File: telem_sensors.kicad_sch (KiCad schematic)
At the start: 45 parts, among them J4 Thermistor Molex, J5 Thermistor Molex, J6 Thermistor Molex, J7 Thermistor Molex, U4 LSM6DSRXTR, U5 MCP6L01x-xLT, U6 MCP6L01x-xLT, U7 BMP585, U8 MCP6L01x-xLT, U9 MCP6L01x-xLT

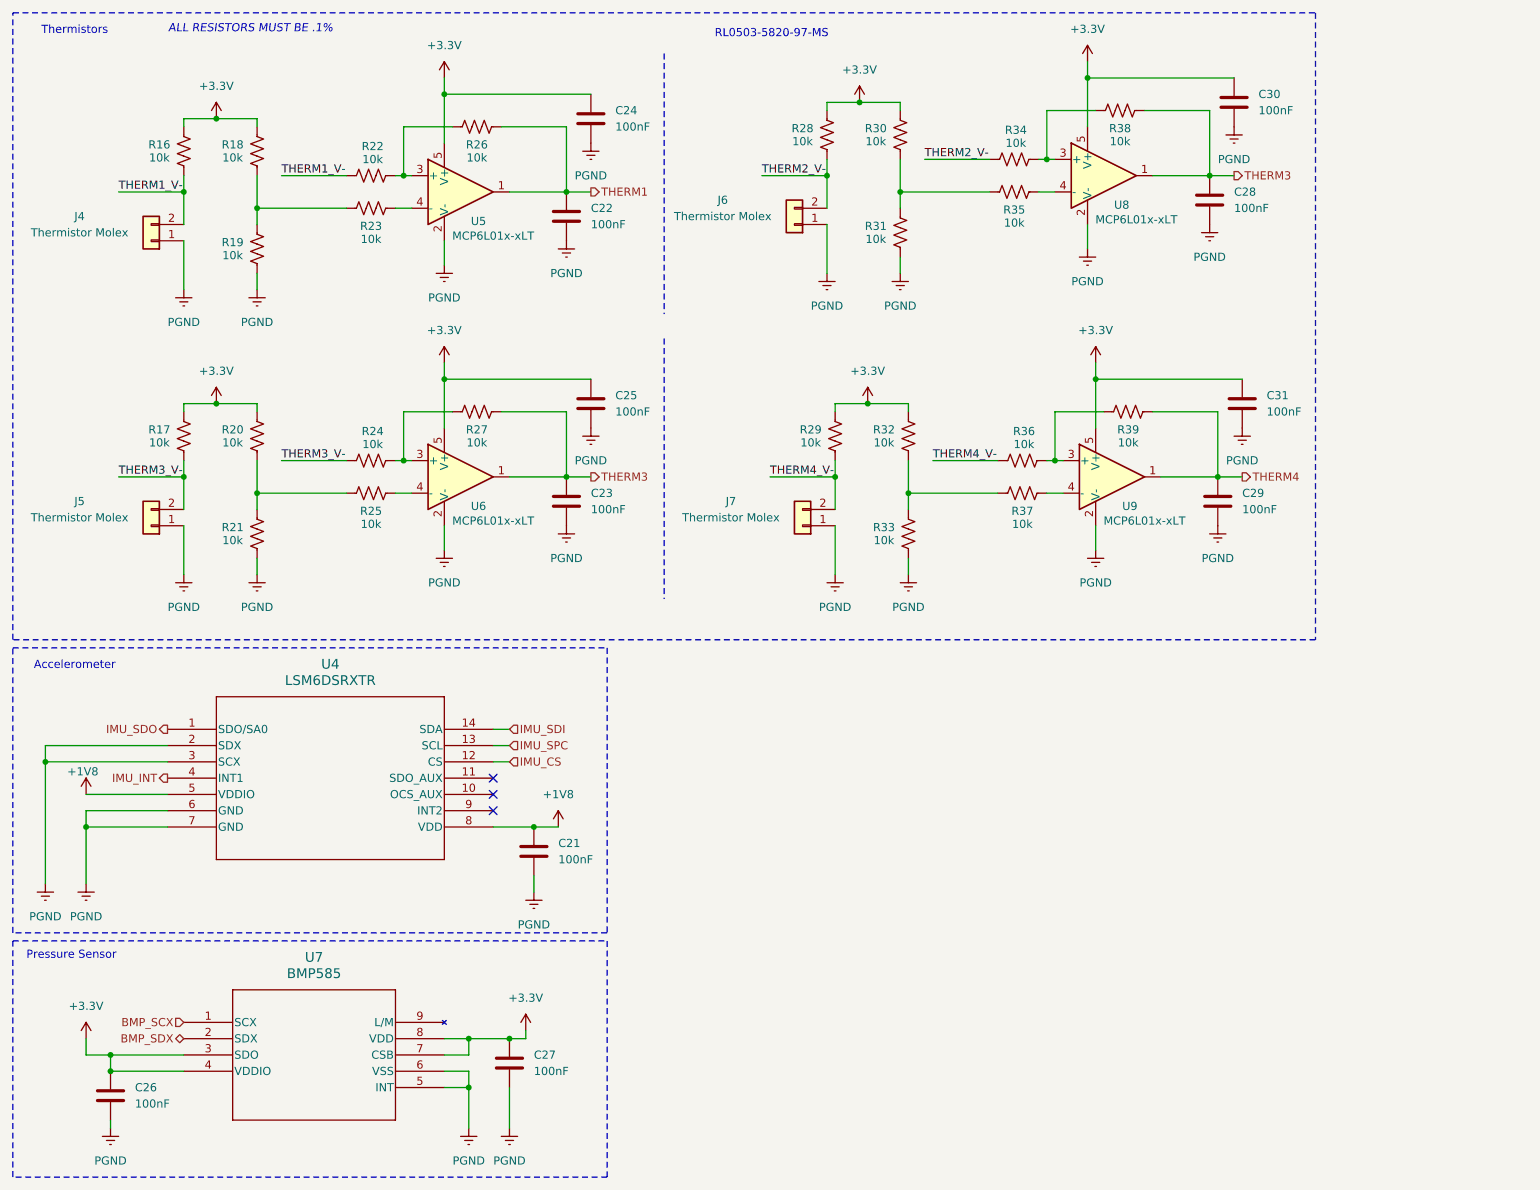
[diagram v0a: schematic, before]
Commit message: Added MAX-M10S GPS, selected antenna and did schematic
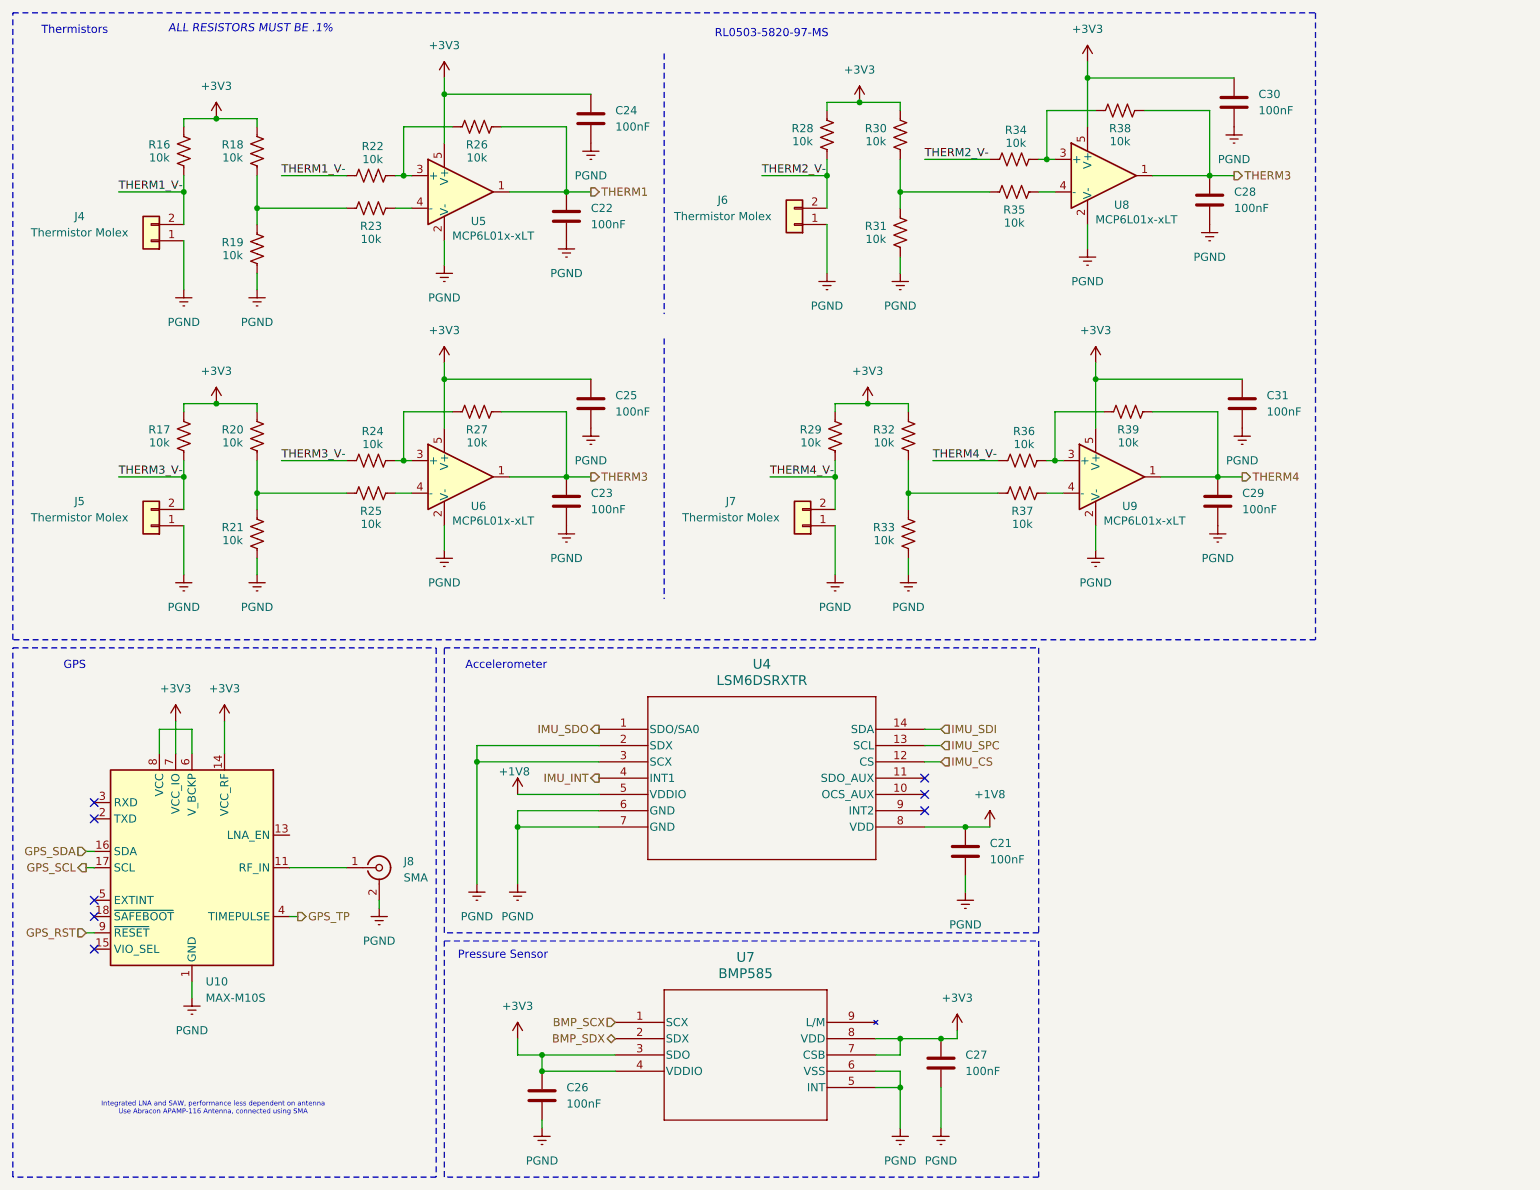
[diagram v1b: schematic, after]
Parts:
- added J8: SMA, Connector_Coaxial:SMA_Amphenol_132289_EdgeMount, symbol Connector:Conn_Coaxial
- added U10: MAX-M10S, RF_GPS:ublox_MAX, symbol RF_GPS:MAX-M10S
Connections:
- net PGND: now also J8.2 (Ext), U10.1 (GND), U10.10 (GND), U10.12 (GND)
- net +3.3V renamed +3V3
- net +3V3: now also U10.14 (VCC_RF), U10.7 (VCC_IO)
- new net: J8.1 (In), U10.11 (RF_IN)
- new net: U10.6 (V_BCKP), U10.8 (VCC)
- new net GPS_RST: U10.9 (~{RESET})
- new net GPS_SCL: U10.17 (SCL)
- new net GPS_SDA: U10.16 (SDA)
- new net GPS_TP: U10.4 (TIMEPULSE)
- no-connect marks 3 -> 8
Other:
- note added: "GPS"
- note added: "Integrated LNA and SAW, performance less dependent on antenna Use Abracon APAMP-116 Antenna, connected using SMA"
- moved on the sheet: C21, C26, C27, U4, U7

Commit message: Schematics complete; Starting layout. Removed 2 thermistors, not necessary. Going to update website once layout starts
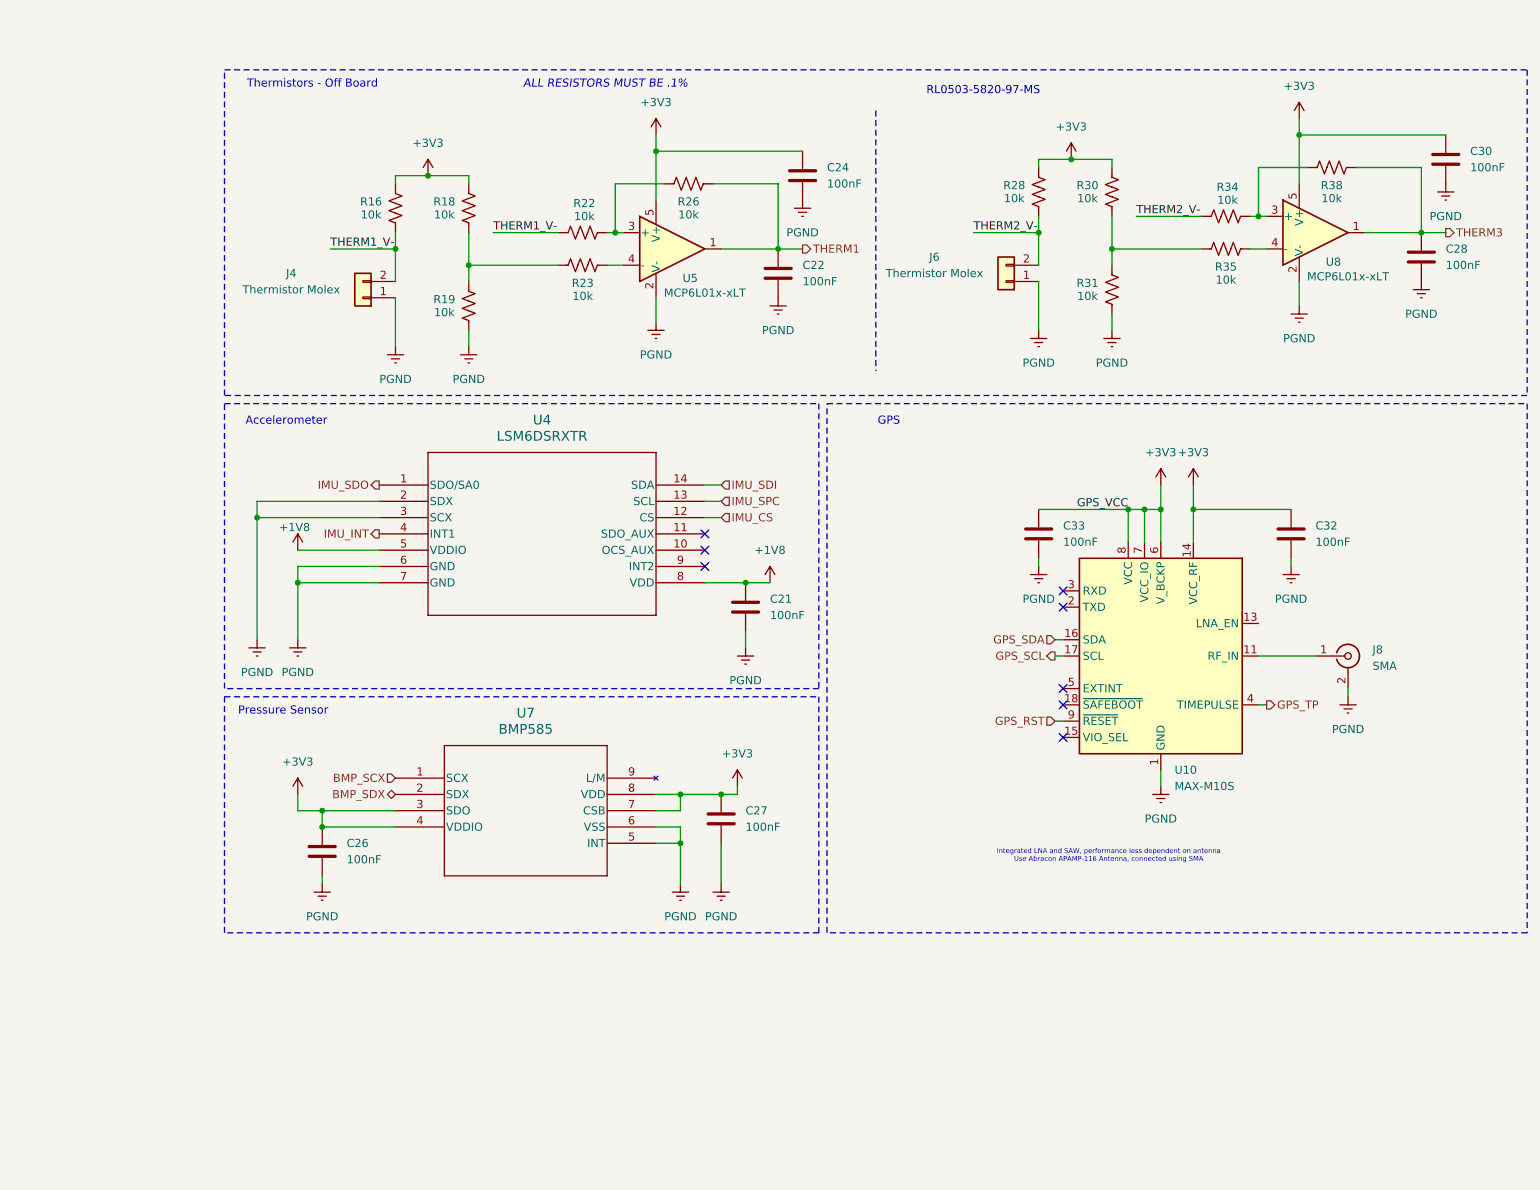
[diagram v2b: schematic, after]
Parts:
- removed C23, C25, C29, C31: 100nF, Capacitor_SMD:C_0805_2012Metric_Pad1.18x1.45mm_HandSolder, symbol Device:C
- removed J5, J7: Thermistor Molex, Connector_Molex:Molex_Micro-Fit_3.0_43650-0200_1x02_P3.00mm_Horizontal, symbol Connector_Generic:Conn_01x02
- removed R17, R20, R21, R24, R25, R27, R29, R32, R33, R36, R37, R39: 10k, Resistor_SMD:R_0603_1608Metric, symbol Device:R_US
- removed U6, U9: MCP6L01x-xLT, Package_TO_SOT_SMD:SOT-353_SC-70-5, symbol Amplifier_Operational:MCP6L01x-xLT
- added C32, C33: 100nF, Capacitor_SMD:C_0805_2012Metric_Pad1.18x1.45mm_HandSolder, symbol Device:C
- J4, J6: footprint Connector_Molex:Molex_Micro-Fit_3.0_43650-0200_1x02_P3.00mm_Horizontal -> Connector_Molex:Molex_MicroClasp_55935-0210_1x02_P2.00mm_Horizontal
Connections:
- net +3V3: now also U10.6 (V_BCKP), U10.8 (VCC), C32.1, C33.1
- net PGND: now also C32.2, C33.2
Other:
- note added: "Thermistors - Off Board"
- note removed: "Thermistors"
- moved on the sheet: C21, C22, C24, C26, C27, C28, C30, J4, J6, J8, R16, R18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

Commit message: Final schematic and initial layout
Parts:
- C21, C26, C27, C32, C33: footprint Capacitor_SMD:C_0805_2012Metric_Pad1.18x1.45mm_HandSolder -> Capacitor_SMD:C_0805_2012Metric
- C22, C24, C28, C30: footprint Capacitor_SMD:C_0805_2012Metric_Pad1.18x1.45mm_HandSolder -> Capacitor_SMD:C_0603_1608Metric
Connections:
- net PGND: now also J4.2 (Pin_2), J6.2 (Pin_2); no longer J4.1 (Pin_1), J6.1 (Pin_1)
- net THERM1_V-: now also J4.1 (Pin_1); no longer J4.2 (Pin_2)
- net THERM2_V-: now also J6.1 (Pin_1); no longer J6.2 (Pin_2)
- net THERM3 renamed THERM2
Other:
- moved on the sheet: J4, J6
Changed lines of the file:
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@@
 	(wire
 		(pts
-			(xy 73.66 58.42) (xy 73.66 66.04)
-		)
-		(stroke
-			(width 0)
-			(type default)
-		)
-	)
-	(wire
-		(pts
 			(xy 185.42 45.72) (xy 185.42 50.8)
 		)
@@
 	(wire
 		(pts
+			(xy 73.66 58.42) (xy 73.66 66.04)
+		)
+		(stroke
+			(width 0)
+			(type default)
+		)
+	)
+	(wire
+		(pts
 			(xy 128.27 110.49) (xy 128.27 113.03)
 		)
@@
 	(wire
 		(pts
+			(xy 173.99 55.88) (xy 173.99 63.5)
+		)
+		(stroke
+			(width 0)
+			(type default)
+		)
+	)
+	(wire
+		(pts
 			(xy 62.23 140.97) (xy 62.23 138.43)
 		)
@@
 	(wire
 		(pts
-			(xy 173.99 55.88) (xy 173.99 63.5)
-		)
-		(stroke
-			(width 0)
-			(type default)
-		)
-	)
-	(wire
-		(pts
 			(xy 118.11 140.97) (xy 118.11 143.51)
 		)
@@
 		)
 	)
-	(hierarchical_label "THERM3"
+	(hierarchical_label "THERM2"
 		(shape output)
 		(at 237.49 48.26 0)
@@
 			)
 		)
-		(property "Footprint" "Capacitor_SMD:C_0805_2012Metric_Pad1.18x1.45mm_HandSolder"
+		(property "Footprint" "Capacitor_SMD:C_0805_2012Metric"
 			(at 129.2352 110.49 0)
 			(hide yes)
@@
 	(symbol
 		(lib_id "Connector_Generic:Conn_01x02")
-		(at 68.58 58.42 180)
+		(at 68.58 55.88 0)
+		(mirror y)
 		(unit 1)
 		(body_style 1)
@@
 		(dnp no)
 		(property "Reference" "J4"
-			(at 57.404 54.61 0)
+			(at 57.404 59.69 0)
 			(show_name no)
 			(do_not_autoplace no)
@@
 		)
 		(property "Footprint" "Connector_Molex:Molex_MicroClasp_55935-0210_1x02_P2.00mm_Horizontal"
-			(at 68.58 58.42 0)
+			(at 68.58 55.88 0)
 			(hide yes)
 			(show_name no)
@@
 		)
 		(property "Datasheet" ""
-			(at 68.58 58.42 0)
+			(at 68.58 55.88 0)
 			(hide yes)
 			(show_name no)
@@
 		)
 		(property "Description" "Generic connector, single row, 01x02, script generated (kicad-library-utils/schlib/autogen/connector/)"
-			(at 68.58 58.42 0)
+			(at 68.58 55.88 0)
 			(hide yes)
 			(show_name no)
@@
 			)
 		)
-		(property "Footprint" "Capacitor_SMD:C_0805_2012Metric_Pad1.18x1.45mm_HandSolder"
+		(property "Footprint" "Capacitor_SMD:C_0805_2012Metric"
 			(at 174.9552 99.06 0)
 			(hide yes)
@@
 			)
 		)
-		(property "Footprint" "Capacitor_SMD:C_0805_2012Metric_Pad1.18x1.45mm_HandSolder"
+		(property "Footprint" "Capacitor_SMD:C_0805_2012Metric"
 			(at 63.1952 148.59 0)
 			(hide yes)
@@
 	(symbol
 		(lib_id "Connector_Generic:Conn_01x02")
-		(at 168.91 55.88 180)
+		(at 168.91 53.34 0)
+		(mirror y)
 		(unit 1)
 		(body_style 1)
@@
 		(dnp no)
 		(property "Reference" "J6"
-			(at 157.734 52.07 0)
+			(at 157.734 57.15 0)
 			(show_name no)
 			(do_not_autoplace no)
@@
 		)
 		(property "Footprint" "Connector_Molex:Molex_MicroClasp_55935-0210_1x02_P2.00mm_Horizontal"
-			(at 168.91 55.88 0)
+			(at 168.91 53.34 0)
 			(hide yes)
 			(show_name no)
@@
 		)
 		(property "Datasheet" ""
-			(at 168.91 55.88 0)
+			(at 168.91 53.34 0)
 			(hide yes)
 			(show_name no)
@@
 		)
 		(property "Description" "Generic connector, single row, 01x02, script generated (kicad-library-utils/schlib/autogen/connector/)"
-			(at 168.91 55.88 0)
+			(at 168.91 53.34 0)
 			(hide yes)
 			(show_name no)
@@
 			)
 		)
-		(property "Footprint" "Capacitor_SMD:C_0805_2012Metric_Pad1.18x1.45mm_HandSolder"
+		(property "Footprint" "Capacitor_SMD:C_0805_2012Metric"
 			(at 125.4252 143.51 0)
 			(hide yes)
@@
 			)
 		)
-		(property "Footprint" "Capacitor_SMD:C_0805_2012Metric_Pad1.18x1.45mm_HandSolder"
+		(property "Footprint" "Capacitor_SMD:C_0603_1608Metric"
 			(at 234.6452 55.88 0)
 			(hide yes)
@@
 			)
 		)
-		(property "Footprint" "Capacitor_SMD:C_0805_2012Metric_Pad1.18x1.45mm_HandSolder"
+		(property "Footprint" "Capacitor_SMD:C_0805_2012Metric"
 			(at 214.3252 99.06 0)
 			(hide yes)
@@
 			)
 		)
-		(property "Footprint" "Capacitor_SMD:C_0805_2012Metric_Pad1.18x1.45mm_HandSolder"
+		(property "Footprint" "Capacitor_SMD:C_0603_1608Metric"
 			(at 138.1252 43.18 0)
 			(hide yes)
@@
 			)
 		)
-		(property "Footprint" "Capacitor_SMD:C_0805_2012Metric_Pad1.18x1.45mm_HandSolder"
+		(property "Footprint" "Capacitor_SMD:C_0603_1608Metric"
 			(at 238.4552 40.64 0)
 			(hide yes)
@@
 			)
 		)
-		(property "Footprint" "Capacitor_SMD:C_0805_2012Metric_Pad1.18x1.45mm_HandSolder"
+		(property "Footprint" "Capacitor_SMD:C_0603_1608Metric"
 			(at 134.3152 58.42 0)
 			(hide yes)

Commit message: Finished initial signal layout
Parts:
- J4, J6: footprint Connector_Molex:Molex_MicroClasp_55935-0210_1x02_P2.00mm_Horizontal -> Connector_Molex:Molex_MicroClasp_55935-0230_1x02_P2.00mm_Horizontal
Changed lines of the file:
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@@
 			)
 		)
-		(property "Footprint" "Connector_Molex:Molex_MicroClasp_55935-0210_1x02_P2.00mm_Horizontal"
+		(property "Footprint" "Connector_Molex:Molex_MicroClasp_55935-0230_1x02_P2.00mm_Horizontal"
 			(at 68.58 55.88 0)
 			(hide yes)
@@
 			)
 		)
-		(property "Footprint" "Connector_Molex:Molex_MicroClasp_55935-0210_1x02_P2.00mm_Horizontal"
+		(property "Footprint" "Connector_Molex:Molex_MicroClasp_55935-0230_1x02_P2.00mm_Horizontal"
 			(at 168.91 53.34 0)
 			(hide yes)

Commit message: Rev1 final commit
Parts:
- C21, C26, C27, C32, C33: footprint Capacitor_SMD:C_0805_2012Metric -> Capacitor_SMD:C_0603_1608Metric
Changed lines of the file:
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@@
 			)
 		)
-		(property "Footprint" "Capacitor_SMD:C_0805_2012Metric"
+		(property "Footprint" "Capacitor_SMD:C_0603_1608Metric"
 			(at 129.2352 110.49 0)
 			(hide yes)
@@
 			)
 		)
-		(property "Footprint" "Capacitor_SMD:C_0805_2012Metric"
+		(property "Footprint" "Capacitor_SMD:C_0603_1608Metric"
 			(at 174.9552 99.06 0)
 			(hide yes)
@@
 			)
 		)
-		(property "Footprint" "Capacitor_SMD:C_0805_2012Metric"
+		(property "Footprint" "Capacitor_SMD:C_0603_1608Metric"
 			(at 63.1952 148.59 0)
 			(hide yes)
@@
 			)
 		)
-		(property "Footprint" "Capacitor_SMD:C_0805_2012Metric"
+		(property "Footprint" "Capacitor_SMD:C_0603_1608Metric"
 			(at 125.4252 143.51 0)
 			(hide yes)
@@
 			)
 		)
-		(property "Footprint" "Capacitor_SMD:C_0805_2012Metric"
+		(property "Footprint" "Capacitor_SMD:C_0603_1608Metric"
 			(at 214.3252 99.06 0)
 			(hide yes)
